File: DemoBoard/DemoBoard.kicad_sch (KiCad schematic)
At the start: 1 part, among them U101 ICM7555xP

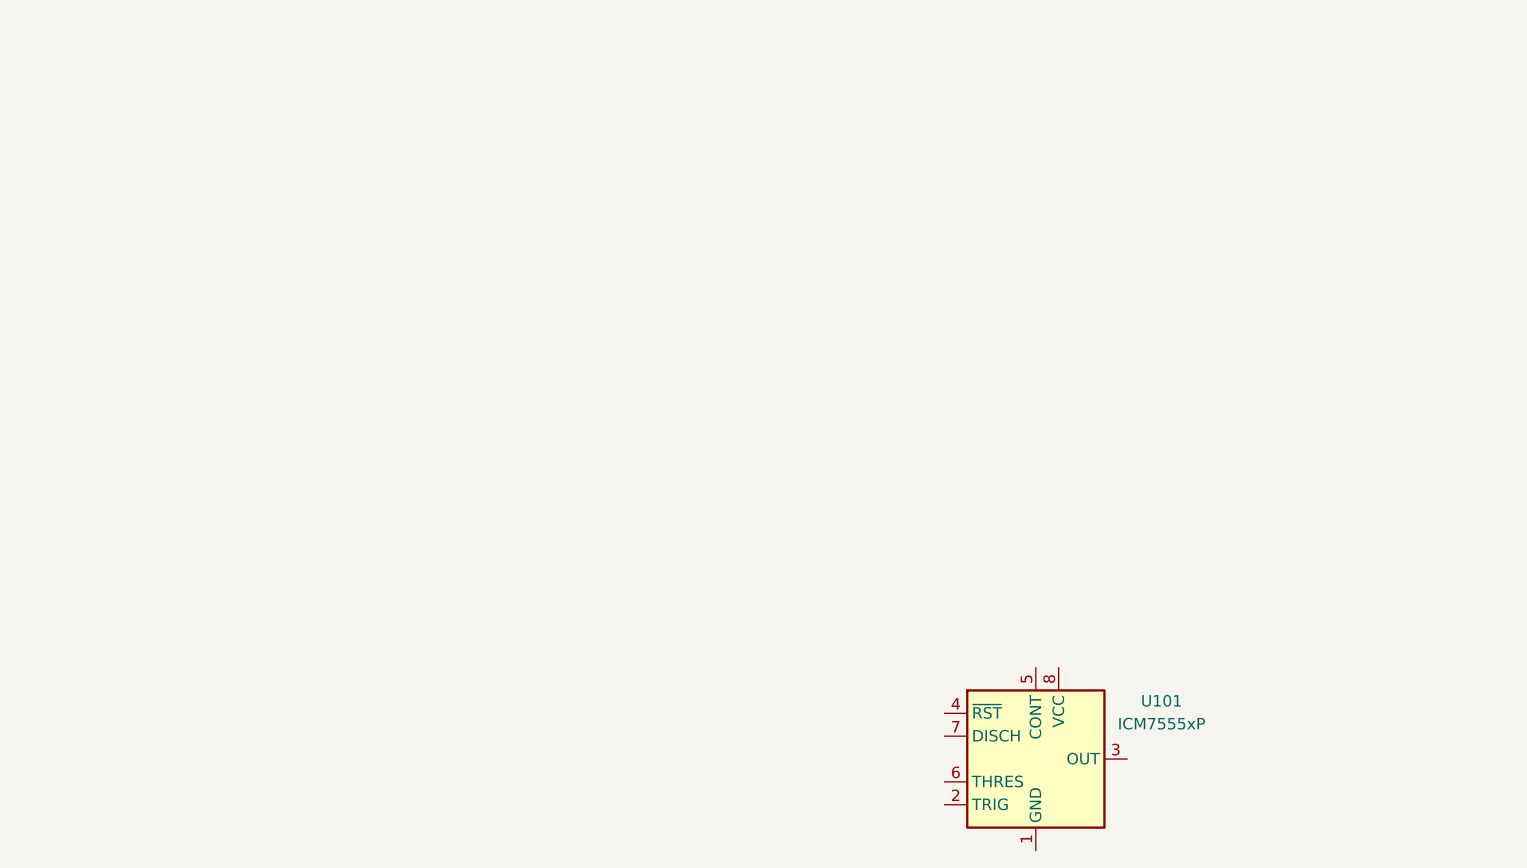
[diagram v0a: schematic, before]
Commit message: Updated 555 Timer + Tunnel Diode (Circuit?)
555 needs resistor ratio + tunnel diode (too expensive?) / what else could be used in its place?
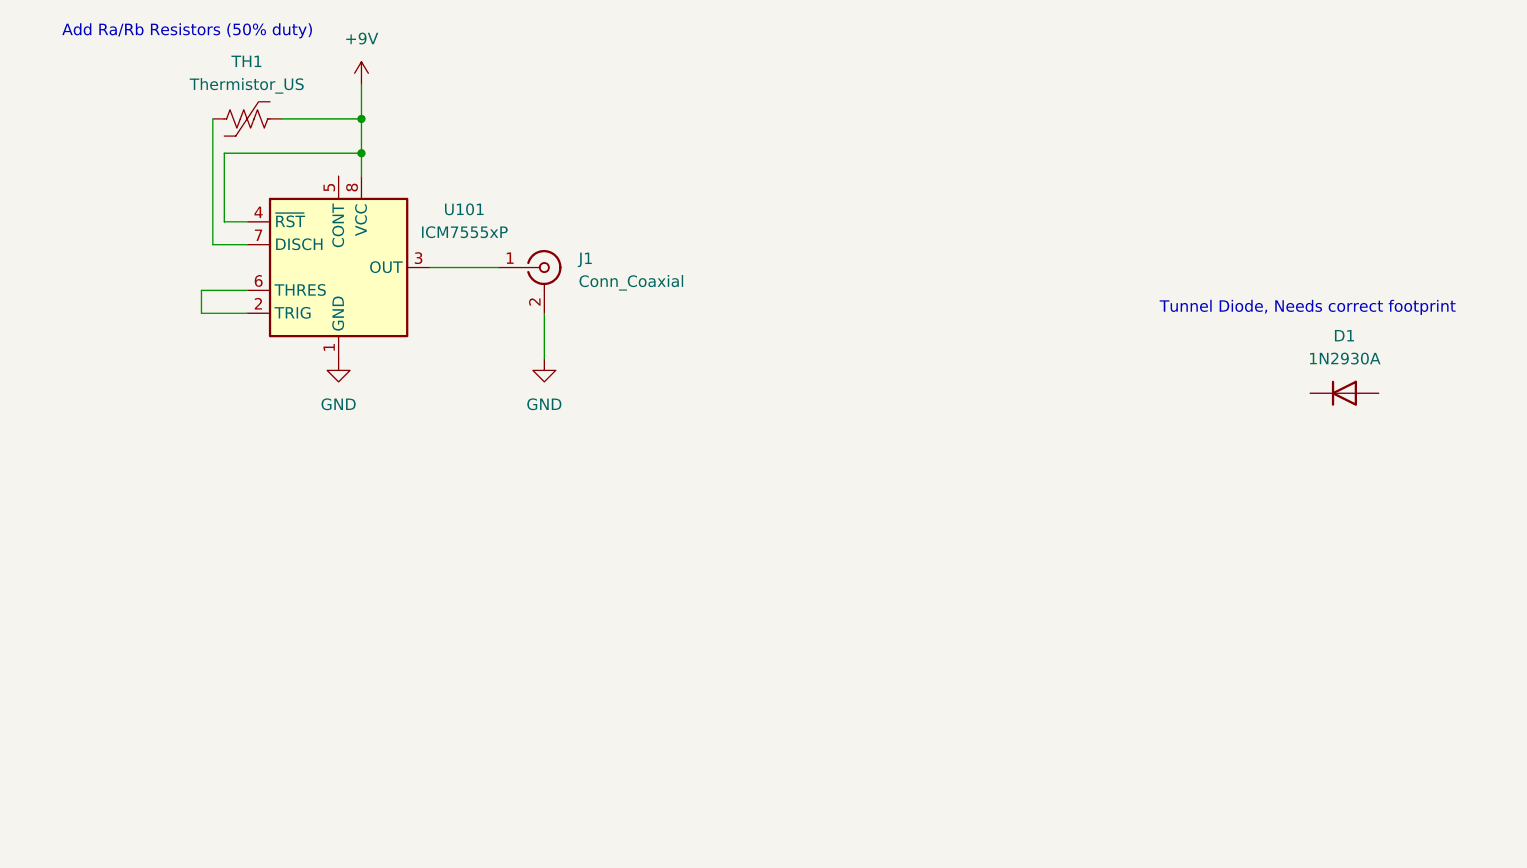
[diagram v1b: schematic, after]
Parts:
- added D1: 1N2930A, symbol Device:D
- added J1: Conn_Coaxial, symbol Connector:Conn_Coaxial
- added TH1: Thermistor_US, symbol Device:Thermistor_US
- U101: LCSC# (none) -> C7432184
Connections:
- net GND: now reaches U101.1 (GND)
- net GND: now also J1.2 (Ext)
- net at U101.2 (TRIG): now also U101.6 (THRES)
- net at U101.3 (OUT): now also J1.1 (In)
- net +9V: now reaches U101.4 (~{RST})
- net +9V: now also U101.8 (VCC), TH1.1
- net at U101.7 (DISCH): now also TH1.2
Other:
- note added: "Add Ra/Rb Resistors (50% duty)"
- note added: "Tunnel Diode, Needs correct footprint"
- moved on the sheet: U101

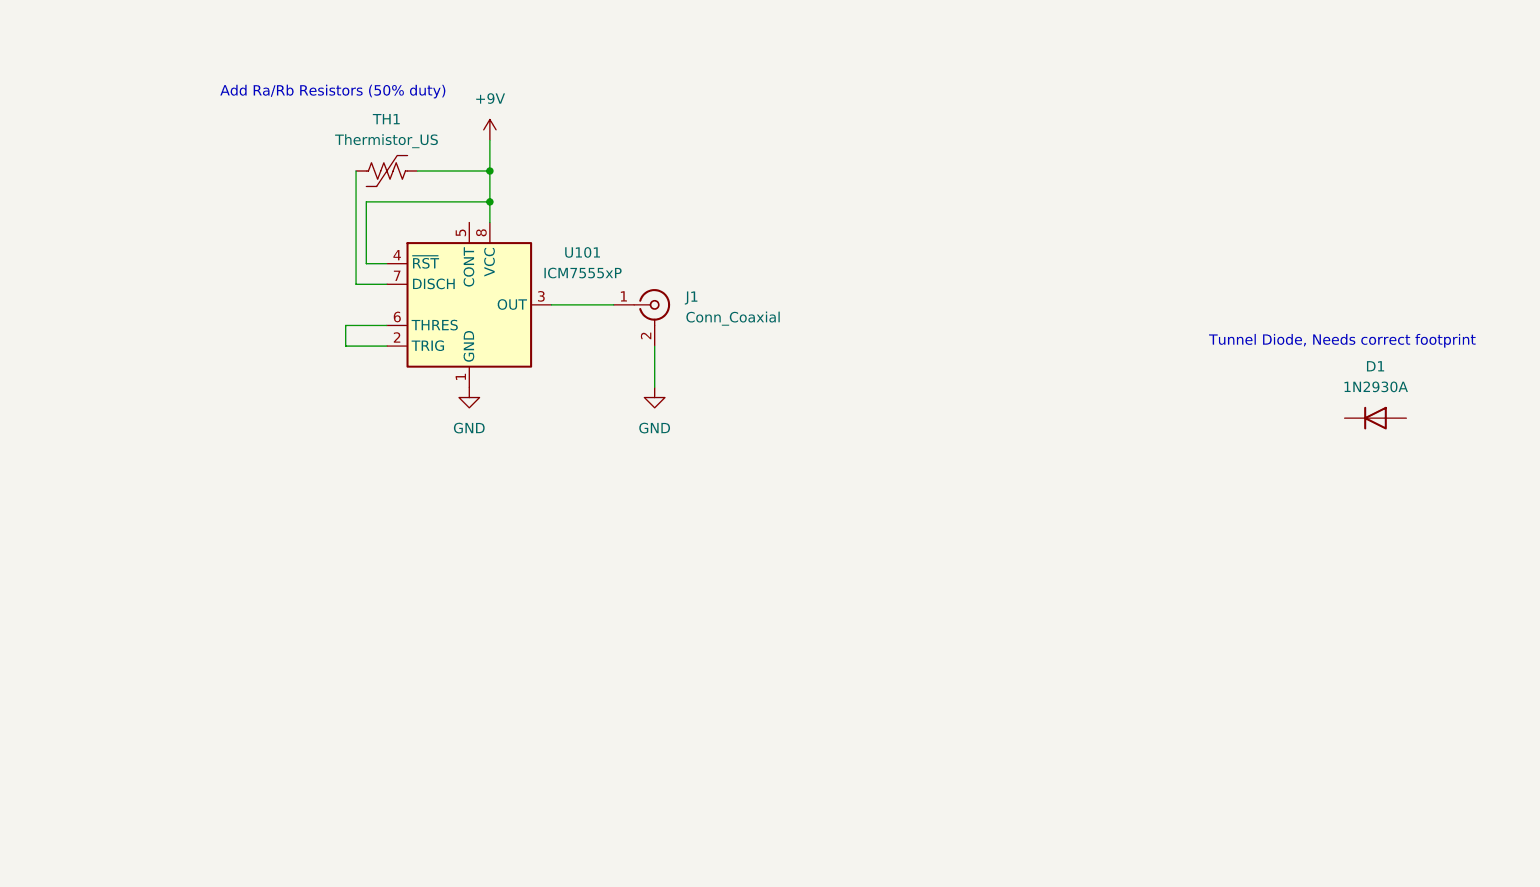
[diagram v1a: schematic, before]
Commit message: Added more blocks for demo testing
Zener + DC Ref
Zener + AC Ref (output of 555)
Base-Emitter breakdown oscillator
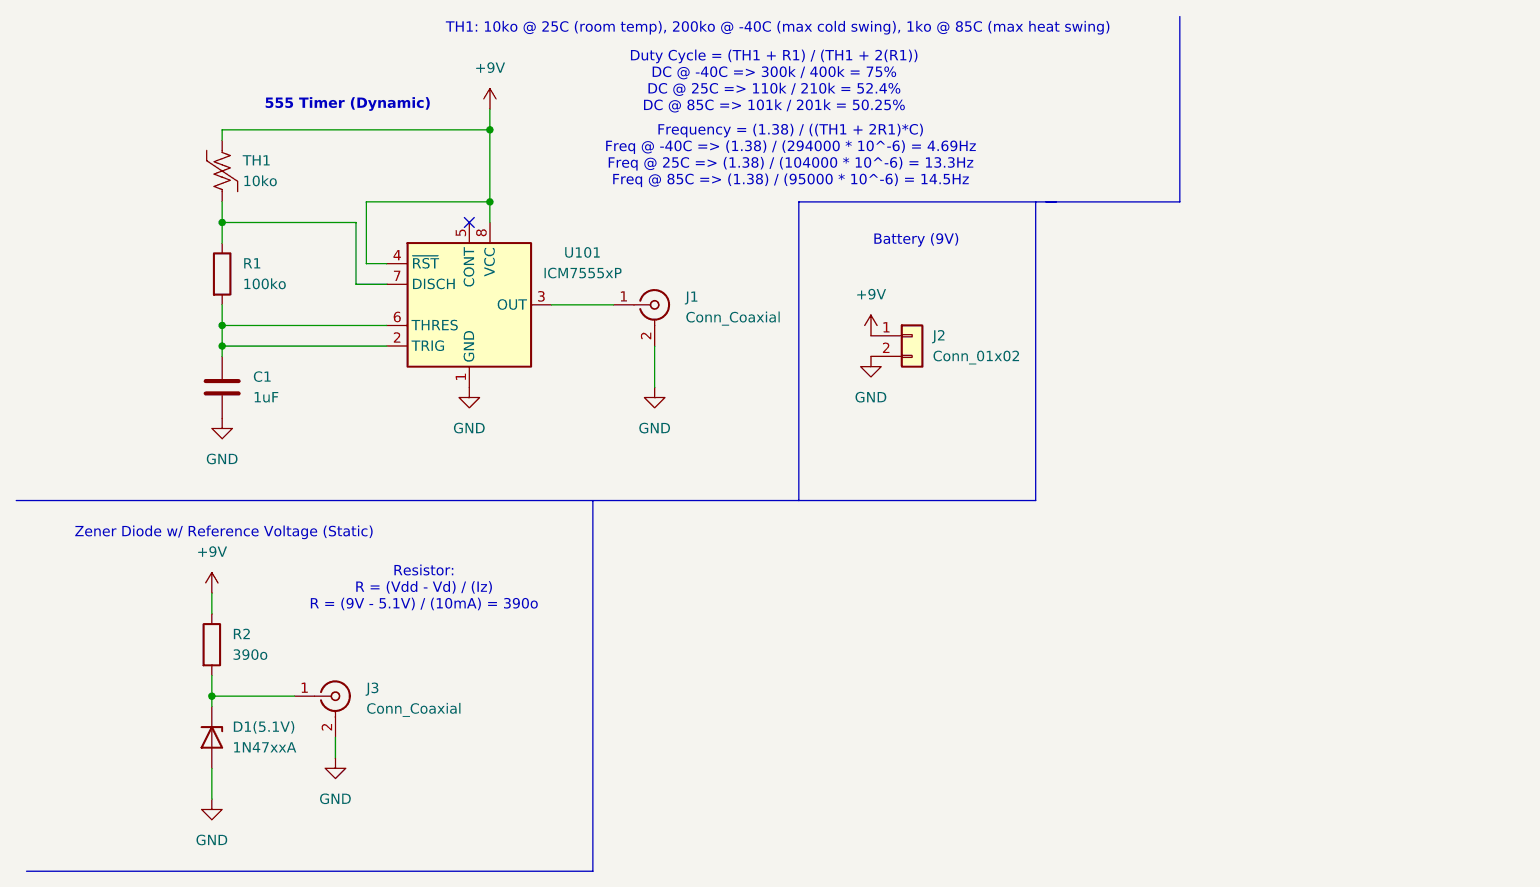
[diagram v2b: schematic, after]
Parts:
- removed D1: 1N2930A, symbol Device:D
- added C1: 1uF, symbol Device:C
- added D1(5.1V): 1N47xxA, Diode_THT:D_DO-41_SOD81_P10.16mm_Horizontal, symbol Diode:1N47xxA
- added J2: Conn_01x02, Connector_Wire:SolderWire-1.5sqmm_1x02_P6mm_D1.7mm_OD3mm_Relief, symbol Connector_Generic:Conn_01x02
- added J3: Conn_Coaxial, symbol Connector:Conn_Coaxial
- added R1: 100ko, symbol Device:R
- added R2: 390o, symbol Device:R
- TH1: value Thermistor_US -> 10ko
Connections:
- net +9V: now also TH1.2, J2.1 (Pin_1), R2.1; no longer TH1.1
- net GND: now also C1.2, D1(5.1V).2 (A), J2.2 (Pin_2), J3.2 (Ext)
- net at U101.2 (TRIG), U101.6 (THRES): now also C1.1, R1.2
- net at U101.7 (DISCH): now also TH1.1, R1.1; no longer TH1.2
- new net: D1(5.1V).1 (K), J3.1 (In), R2.2
- no-connect marks 0 -> 1
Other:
- note added: "555 Timer (Dynamic)"
- note added: "Battery (9V)"
- note added: "Duty Cycle = (TH1 + R1) / (TH1 + 2(R1)) DC @ -40C => 300k / 400k = 75% DC @ 25C => 110k / 210k = 52.4% DC @ 85C => 101k / 201k = 50.25%"
- note added: "Frequency = (1.38) / ((TH1 + 2R1)*C) Freq @ -40C => (1.38) / (294000 * 10^-6) = 4.69Hz Freq @ 25C => (1.38) / (104000 * 10^-6) = 13.3Hz Freq @ 85C => (1.38) / (95000 * 10^-6) = 14.5Hz"
- note added: "Resistor: R = (Vdd - Vd) / (Iz) R = (9V - 5.1V) / (10mA) = 390o"
- note added: "TH1: 10ko @ 25C (room temp), 200ko @ -40C (max cold swing), 1ko @ 85C (max heat swing)"
- note added: "Zener Diode w/ Reference Voltage (Static)"
- note removed: "Add Ra/Rb Resistors (50% duty)"
- note removed: "Tunnel Diode, Needs correct footprint"
- moved on the sheet: TH1

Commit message: Added a comment
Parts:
- added C2, C3, C4: 1uF, symbol Device:C
- added C5: 0.1uF, symbol Device:C
- added D1(5.1V)1: 1N47xxA, Diode_THT:D_DO-41_SOD81_P10.16mm_Horizontal, symbol Diode:1N47xxA
- added J4, J5: Conn_Coaxial, symbol Connector:Conn_Coaxial
- added Q1: 2N3904, Package_TO_SOT_THT:TO-92_Inline, symbol Transistor_BJT:2N3904
- added R3: 100ko, symbol Device:R
- added R4: 2.2ko, symbol Device:R
- added R5: 560ko, symbol Device:R
- added TH2: 10ko, symbol Device:Thermistor_US
- added U1: ICM7555xP, Package_DIP:DIP-8_W7.62mm, symbol Timer:ICM7555xP
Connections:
- net +9V: now also R5.1, TH2.2, U1.4 (~{RST}), U1.8 (VCC)
- net GND: now also C2.2, C3.2, C4.2, D1(5.1V)1.2 (A), J4.2 (Ext), J5.2 (Ext), Q1.1 (E), U1.1 (GND)
- net at D1(5.1V).1 (K), J3.1 (In), R2.2: now also C3.1
- new net: C5.1, J5.1 (In), R5.2
- new net: C2.1, R3.2, U1.2 (TRIG), U1.6 (THRES)
- new net: R3.1, TH2.1, U1.7 (DISCH)
- new net: C4.1, D1(5.1V)1.1 (K), R4.1
- new net: C5.2, Q1.2 (B)
- new net: J4.1 (In), R4.2, U1.3 (OUT)
- no-connect marks 1 -> 3
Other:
- note added: "(Base-Emitter) Breakdown Oscillator"
- note added: "555 Timer + Zener (Nonlinear Clipper)"
- note added: "Ceramic"
- note added: "Demonstrates oscillation governed by base-emitter junction breakdown. Temperature influenced shifts in breakdown voltage alter threshold triggering, result in frequency and waveform amplitude changes."
- note added: "Demonstrates temperature-sensitive nonlinear voltage limiting. Variations in Zener breakdown modify waveform clipping behavior, producing changes in waveform geometry."
- note added: "Noise Decoupling Ceramic"
- note added: "Provides a DC voltage reference to show Zener breakdown behavior. As temperature swings, shifts in the reference voltage occur due to semiconductor band effects."
- note added: "Resistor: Vbe(breakdown) = ~7.5V ln((9)/(9-7.5)) = ~1.79 Want f = 10Hz T = 1.79RC RC = 0.056 Choose C = 0.1uF R = (0.056) / (0.1uF) = 560ko"
- note added: "Shows temperature-dependent resistances changing RC timing behavior. As temperature varies, the oscillation frequency and duty cycle shift due to changes in capacitor charge/discharge."
- note added: "Zener Clipping: Iz = (Vin - Vz) / (R) For soft knee: Iz >= Iz(min) AND R <= (Vin(max) - Vz) / (Iz(min)) ... so, (Vin(max) - Vz) / (Iz(max)) <= R <= (Vin(max) - Vz) / (Iz(min)) [Lower Bound]: R >= (9V - 3.3V) / (20mA) = |R >= 285| [Upper Bound]: R <= (9V - 3.3V) / (1mA) = |R <= 5700| ...so 285 <= R <= 5.7k ... choose 2.2ko"
- note added: "Zener Diode w/ DC Reference Voltage (Static)"
- note removed: "Zener Diode w/ Reference Voltage (Static)"
- moved on the sheet: C1, D1(5.1V), J1, J2, J3, R1, R2, U101

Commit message: Add KHDA BNC connector from upstream, include/pop P/N in sch sheet
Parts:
- J1, J3, J4, J5: footprint (none) -> thermocline:HL-BNC-KHDA; LCSC# (none) -> C19712152
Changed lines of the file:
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@@
 			)
 		)
-		(property "Footprint" ""
+		(property "Footprint" "thermocline:HL-BNC-KHDA"
 			(at 184.15 39.37 0)
 			(effects
@@
 			)
 		)
-		(property "Datasheet" "~"
+		(property "Datasheet" "https://www.lcsc.com/datasheet/C19712152.pdf"
 			(at 184.15 39.37 0)
 			(effects
@@
 			)
 		)
+		(property "LCSC#" "C19712152"
+			(at 184.15 39.37 0)
+			(effects
+				(font
+					(size 1.27 1.27)
+				)
+				(hide yes)
+			)
+		)
 		(pin "1"
 		)
@@
 			)
 		)
-		(property "Footprint" ""
+		(property "Footprint" "thermocline:HL-BNC-KHDA"
 			(at 90.17 45.72 0)
 			(effects
@@
 			)
 		)
-		(property "Datasheet" "~"
+		(property "Datasheet" "https://www.lcsc.com/datasheet/C19712152.pdf"
 			(at 90.17 45.72 0)
 			(effects
@@
 			)
 		)
+		(property "LCSC#" "C19712152"
+			(at 90.17 45.72 0)
+			(effects
+				(font
+					(size 1.27 1.27)
+				)
+				(hide yes)
+			)
+		)
 		(pin "1"
 		)
@@
 	)
 	(symbol
+		(lib_id "thermocline-symbols:Team Thermocline Logo")
+		(at 284.48 181.61 0)
+		(unit 1)
+		(exclude_from_sim no)
+		(in_bom yes)
+		(on_board yes)
+		(dnp no)
+		(fields_autoplaced yes)
+		(property "Reference" "#G101"
+			(at 269.24 176.4736 0)
+			(effects
+				(font
+					(size 1.27 1.27)
+				)
+				(hide yes)
+			)
+		)
+		(property "Value" "Team Thermocline Logo"
+			(at 269.24 180.34 0)
+			(effects
+				(font
+					(size 1.27 1.27)
+				)
+				(hide yes)
+			)
+		)
+		(property "Footprint" ""
+			(at 269.24 178.4068 0)
+			(effects
+				(font
+					(size 1.27 1.27)
+				)
+				(hide yes)
+			)
+		)
+		(property "Datasheet" ""
+			(at 269.24 178.4068 0)
+			(effects
+				(font
+					(size 1.27 1.27)
+				)
+				(hide yes)
+			)
+		)
+		(property "Description" ""
+			(at 269.24 178.4068 0)
+			(effects
+				(font
+					(size 1.27 1.27)
+				)
+				(hide yes)
+			)
+		)
+		(instances
+			(project ""
+				(path "/894f620e-3404-4a40-a2a7-513bc1d5f99b"
+					(reference "#G101")
+					(unit 1)
+				)
+			)
+		)
+	)
+	(symbol
 		(lib_id "power:GND")
 		(at 139.7 33.02 0)
@@
 			)
 		)
-		(property "Footprint" ""
+		(property "Footprint" "thermocline:HL-BNC-KHDA"
 			(at 58.42 99.06 0)
 			(effects
@@
 			)
 		)
-		(property "Datasheet" "~"
+		(property "Datasheet" "https://www.lcsc.com/datasheet/C19712152.pdf"
 			(at 58.42 99.06 0)
 			(effects
@@
 			)
 		)
+		(property "LCSC#" "C19712152"
+			(at 58.42 99.06 0)
+			(effects
+				(font
+					(size 1.27 1.27)
+				)
+				(hide yes)
+			)
+		)
 		(pin "1"
 		)
@@
 			)
 		)
-		(property "Footprint" ""
+		(property "Footprint" "thermocline:HL-BNC-KHDA"
 			(at 100.33 162.56 0)
 			(effects
@@
 			)
 		)
-		(property "Datasheet" "~"
+		(property "Datasheet" "https://www.lcsc.com/datasheet/C19712152.pdf"
 			(at 100.33 162.56 0)
 			(effects
@@
 			)
 		)
+		(property "LCSC#" "C19712152"
+			(at 100.33 162.56 0)
+			(effects
+				(font
+					(size 1.27 1.27)
+				)
+				(hide yes)
+			)
+		)
 		(pin "1"
 		)
@@
 					(unit 1)
 				)
+			)
+		)
+	)
+	(symbol
+		(lib_id "thermocline-symbols:SNHU_LOGO")
+		(at 243.84 177.8 0)
+		(unit 1)
+		(exclude_from_sim no)
+		(in_bom yes)
+		(on_board yes)
+		(dnp no)
+		(fields_autoplaced yes)
+		(property "Reference" "#G102"
+			(at 243.84 173.1913 0)
+			(effects
+				(font
+					(size 1.27 1.27)
+				)
+				(hide yes)
+			)
+		)
+		(property "Value" "SNHU_LOGO"
+			(at 243.84 182.4087 0)
+			(effects
+				(font
+					(size 1.27 1.27)
+				)
+				(hide yes)
+			)
+		)
+		(property "Footprint" ""
+			(at 243.84 177.8 0)
+			(effects
+				(font
+					(size 1.27 1.27)
+				)
+				(hide yes)
+			)
+		)
+		(property "Datasheet" ""
+			(at 243.84 177.8 0)
+			(effects
+				(font
+					(size 1.27 1.27)
+				)
+				(hide yes)
+			)
+		)
+		(property "Description" ""
+			(at 243.84 177.8 0)
+			(effects
+				(font
+					(size 1.27 1.27)
+				)
+				(hide yes)
+			)
+		)
+		(instances
+			(project ""
+				(path "/894f620e-3404-4a40-a2a7-513bc1d5f99b"
+					(reference "#G102")
+					(unit 1)
+				)
